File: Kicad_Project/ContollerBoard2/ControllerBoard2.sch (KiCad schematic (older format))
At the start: 36 parts, among them J1 Main Header, J2 SWD, J3 WD_Disable, Q1 BSS84, U1 FS32K116

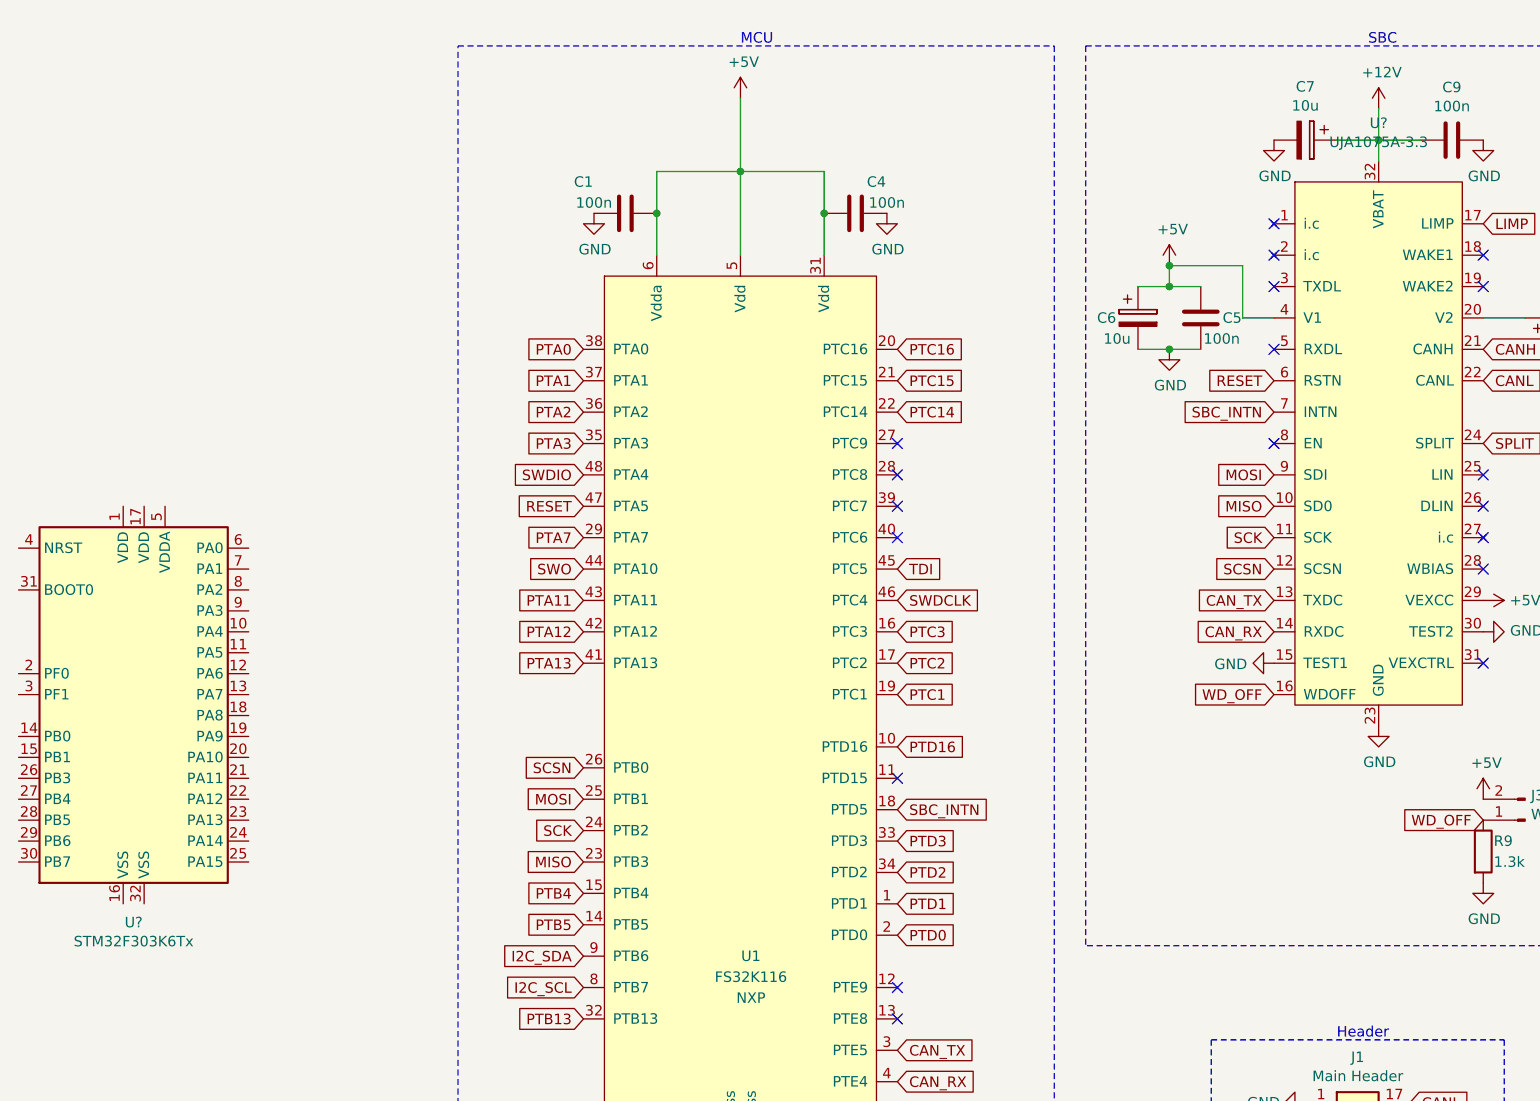
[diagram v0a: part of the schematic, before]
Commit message: Brought PCBNew document over from v1
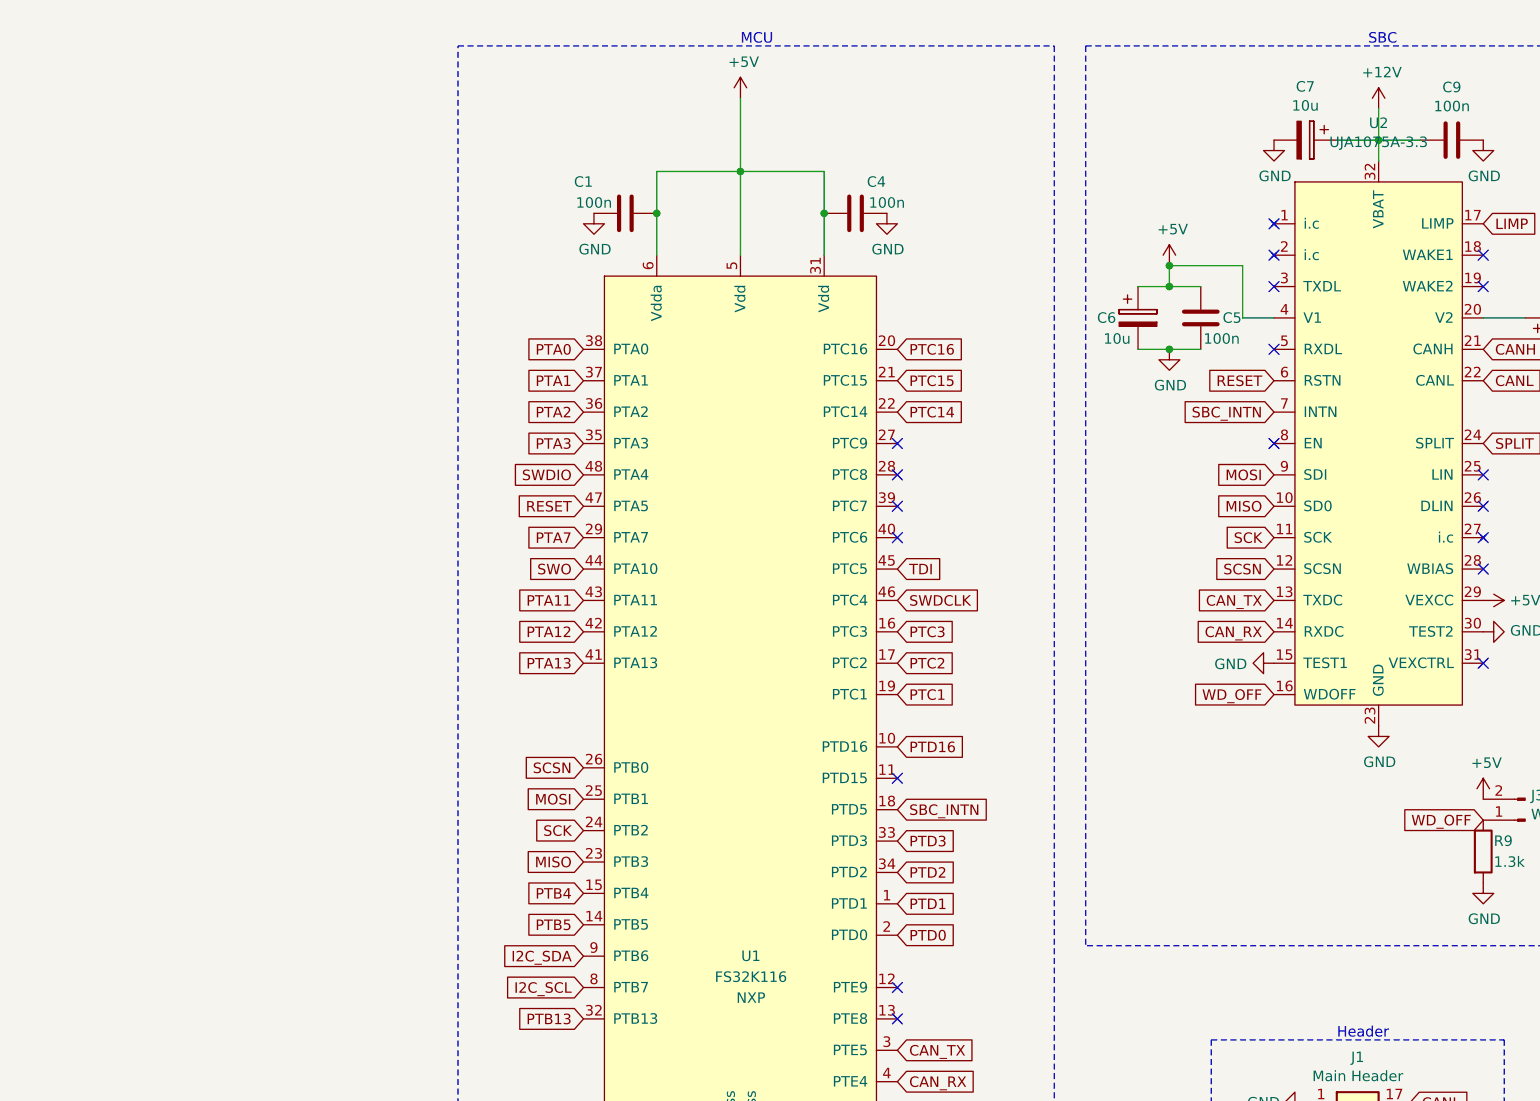
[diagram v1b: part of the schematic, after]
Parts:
- removed U?: STM32F303K6Tx, Package_QFP:LQFP-32_7x7mm_P0.8mm, symbol MCU_ST_STM32F3:STM32F303K6Tx
- gave numbers to parts that had none: 1
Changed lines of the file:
@@
 EESchema Schematic File Version 4
+LIBS:ControllerBoard2-cache
 EELAYER 30 0
 EELAYER END
@@
 $EndComp
 $Comp
-L MCU_ST_STM32F3:STM32F303K6Tx U?
-U 1 1 5F6908E6
-P -900 3900
-F 0 "U?" H -950 2811 50  0000 C CNN
-F 1 "STM32F303K6Tx" H -950 2720 50  0000 C CNN
-F 2 "Package_QFP:LQFP-32_7x7mm_P0.8mm" H -1400 3000 50  0001 R CNN
-F 3 "http://www.st.com/st-web-ui/static/active/en/resource/technical/document/datasheet/DM00092070.pdf" H -900 3900 50  0001 C CNN
-	1    -900 3900
-	1    0    0    -1
-$EndComp
-$Comp
-L Lukas_Library:UJA1075A-3.3 U?
+L Lukas_Library:UJA1075A-3.3 U2
 U 1 1 5F69D58B
 P 5000 1650
-F 0 "U?" H 5000 2131 50  0000 C CNN
+F 0 "U2" H 5000 2131 50  0000 C CNN
 F 1 "UJA1075A-3.3" H 5000 2040 50  0000 C CNN
 F 2 "Package_SO:TSSOP-32_6.1x11mm_P0.65mm" H 5100 -850 50  0001 C CNN

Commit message: First draft of controlboard2
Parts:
- removed C5: 100n, Capacitor_SMD:C_0603_1608Metric_Pad1.05x0.95mm_HandSolder, symbol Device:C
- removed C8: 4.7n, Capacitor_SMD:C_0805_2012Metric_Pad1.15x1.40mm_HandSolder, symbol Device:C
- removed R3, R4: 1.3k, Resistor_SMD:R_0603_1608Metric_Pad1.05x0.95mm_HandSolder, symbol Device:R
- removed U1: FS32K116, digikey-footprints:LQFP-48_7x7mm, symbol Lukas_Library:FS32K116
- added C2, C3: 18p, Capacitor_SMD:C_0603_1608Metric_Pad1.05x0.95mm_HandSolder, symbol Device:C
- added U1: STM32F303K8Tx, Package_QFP:LQFP-32_7x7mm_P0.8mm, symbol MCU_ST_STM32F3:STM32F303K8Tx
- added Y1: 8Mhz, Crystal:Crystal_SMD_Abracon_ABM3-2Pin_5.0x3.2mm_HandSoldering, symbol Device:Crystal
- U2: footprint Package_SO:TSSOP-32_6.1x11mm_P0.65mm -> Package_SO:HTSSOP-32-1EP_6.1x11mm_P0.65mm_EP5.2x11mm_Mask4.11x4.36mm_ThermalVias
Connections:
- net +5V: no longer C1.2, C4.1, C6.1, D1.2 (A), D5.2 (A), J2.1 (Pin_1), J3.2 (Pin_2), Q1.2 (D), R1.1, R13.1, R5.1, R6.1, R7.1, U2.29 (VEXCC), U2.4 (V1)
- net CAN_RX: now also U1.21 (PA11)
- net CAN_TX: now also U1.22 (PA12)
- net GND: now also C2.2, C3.2, U1.16 (VSS), U1.32 (VSS)
- net MISO: now also U1.12 (PA6)
- net MOSI: now also U1.13 (PA7)
- net RESET: now also U1.4 (NRST)
- net SCK: now also U1.11 (PA5)
- net SCSN: now also U1.10 (PA4)
- net SWDCLK: now also U1.24 (PA14)
- net SWDIO: now also U1.23 (PA13)
- net SWO: now also U1.26 (PB3)
- net TDI: now also U1.25 (PA15)
- net I2C_SCL: no longer names the net of J1.13 (Pin_13)
- net I2C_SDA: no longer names the net of J1.12 (Pin_12)
- net PTA0: no longer names the net of J1.15 (Pin_15)
- net PTA1: no longer names the net of J1.14 (Pin_14)
- net PTA11: no longer names the net of J1.16 (Pin_16)
- net PTA12: no longer names the net of D3.2 (A)
- net PTA13: no longer names the net of D2.2 (A)
- net PTA2: no longer names the net of J1.10 (Pin_10)
- net PTA3: no longer names the net of J1.9 (Pin_9)
- net PTA7: no longer names the net of J1.11 (Pin_11)
- net PTB13: no longer names the net of J1.6 (Pin_6)
- net PTB4 renamed PF0
- net PTB5 renamed PB7
- net PB7: now also U1.30 (PB7)
- net PTC1 renamed PA1
- net PA1: now also U1.7 (PA1)
- net PTC14: no longer names the net of J1.21 (Pin_21)
- net PTC15 renamed PA3
- net PA3: now also U1.9 (PA3)
- net PTC16 renamed PA2
- net PA2: now also U1.8 (PA2)
- net PTC2 renamed PA0
- net PA0: now also U1.6 (PA0)
- net PTC3 renamed PF1
- net PTD0 renamed PB5
- net PB5: now also U1.28 (PB5)
- net PTD1 renamed PB4
- net PB4: now also U1.27 (PB4)
- net PTD16 renamed PB6
- net PB6: now also U1.29 (PB6)
- net PTD2: no longer names the net of J1.8 (Pin_8)
- net PTD3: no longer names the net of J1.7 (Pin_7)
- new net +3V3: C1.2, C4.1, C6.1, D1.2 (A), D5.2 (A), J2.1 (Pin_1), J3.2 (Pin_2), Q1.2 (D), R1.1, R13.1, R5.1, R6.1, R7.1, U1.1 (VDD), U1.17 (VDD), U1.5 (VDDA), U2.29 (VEXCC), U2.4 (V1)
- new net OSC_IN: C2.1, U1.2 (PF0), Y1.1
- new net OSC_OUT: C3.1, U1.3 (PF1), Y1.2
- new net PA10: U1.20 (PA10)
- new net PA8: U1.18 (PA8)
- new net PA9: U1.19 (PA9)
- new net PB0: U1.14 (PB0)
- new net PB1: U1.15 (PB1)
- no-connect marks 21 -> 15
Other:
- moved on the sheet: C1, C4, C6
